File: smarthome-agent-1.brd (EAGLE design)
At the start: 100 x 80 mm, 7 parts, among them IC2 7808T, Q1 16Mhz, U1 ATMEGA328P_PDIP_EZ

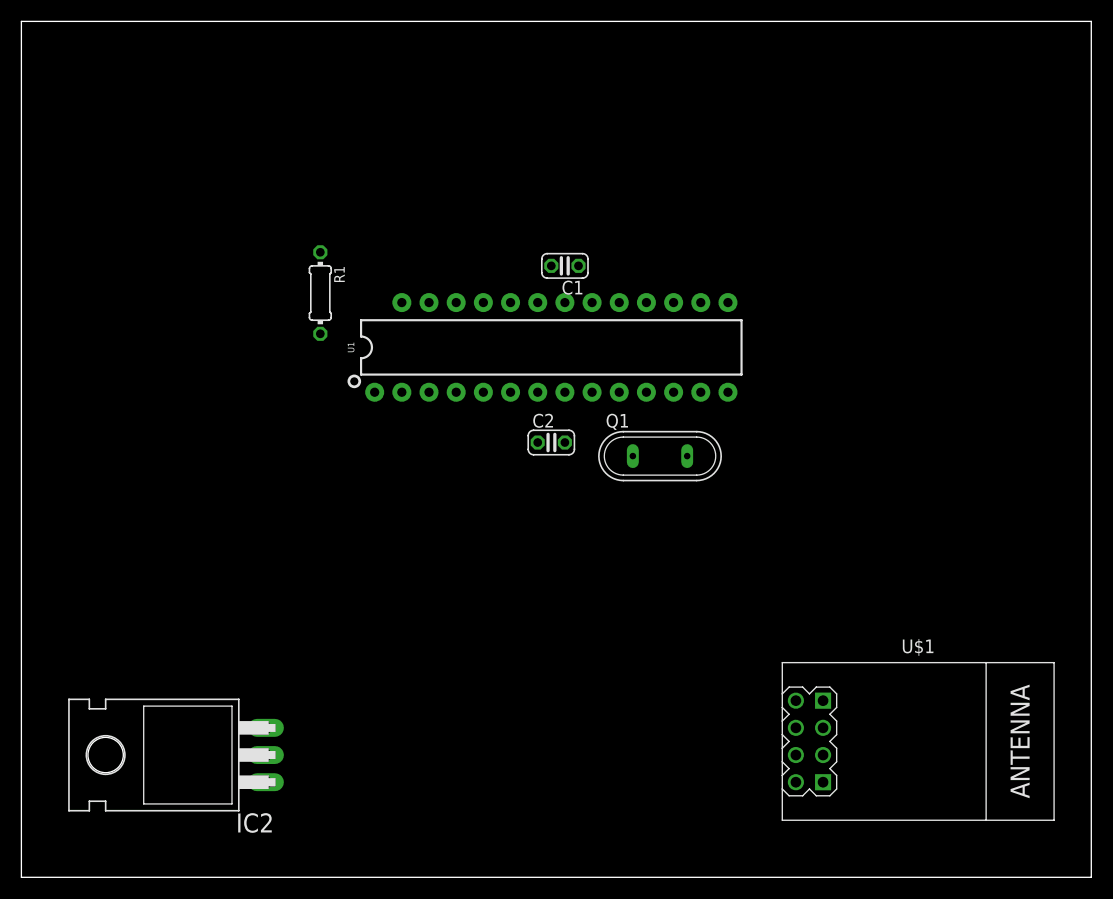
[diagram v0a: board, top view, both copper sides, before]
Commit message: Add board
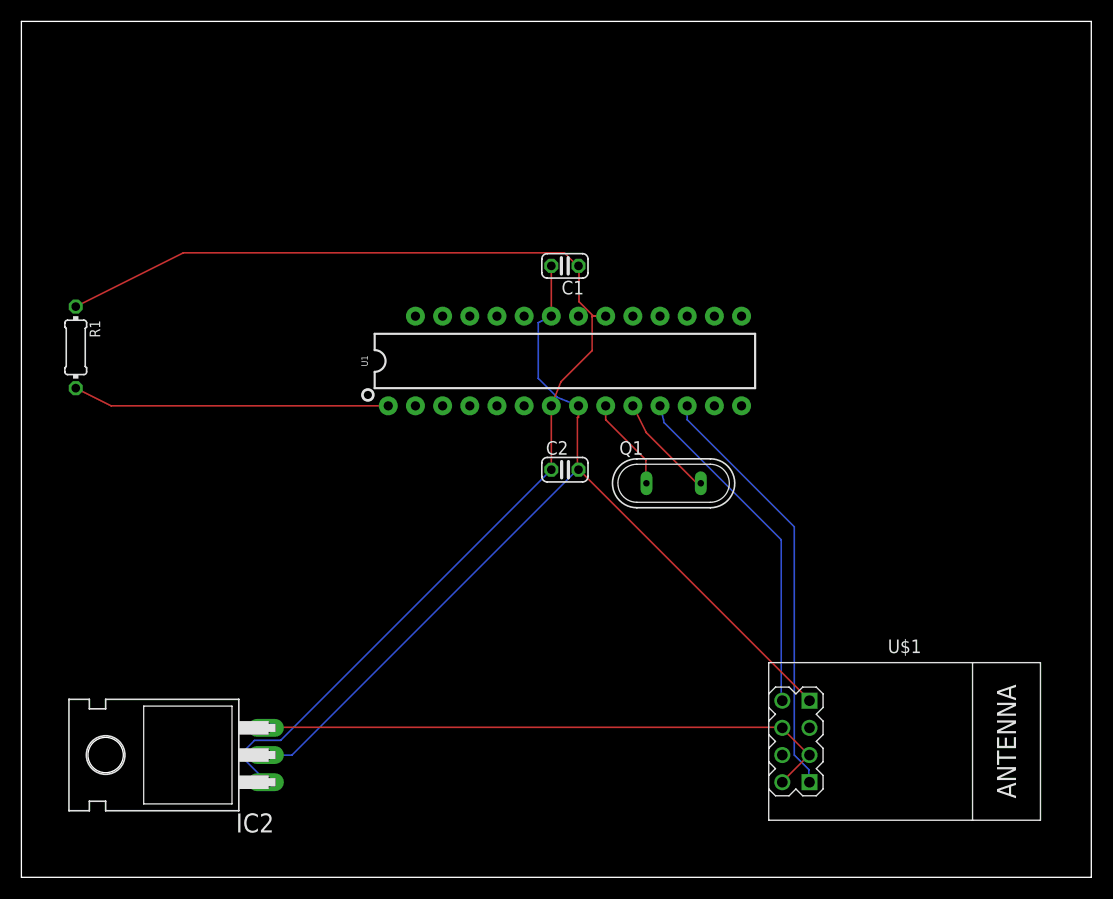
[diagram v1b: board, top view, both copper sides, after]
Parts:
- moved R1 23.4 mm to (5.08, 49.5)
- moved Q1 2.84 mm to (61.0, 36.8)
- moved C2 2.84 mm to (50.8, 38.1)
- moved U1 1.80 mm to (50.8, 48.3)
- moved U$1 1.27 mm to (82.5, 12.7)
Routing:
- net VCC: track 0.00 -> 115.4 mm
- net AGND: track 0.00 -> 92.9 mm
- net N$2: track 0.00 -> 55.5 mm
- net N$6: track 0.00 -> 39.9 mm
- net N$5: track 0.00 -> 32.2 mm
- net N$1: track 0.00 -> 29.6 mm
- net N$4: track 0.00 -> 9.85 mm
- net N$3: track 0.00 -> 8.82 mm

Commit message: Update board to use one layer
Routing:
- net AGND: track 92.9 -> 127.9 mm
- net VCC: track 115.4 -> 122.5 mm
- net N$6: track 39.9 -> 42.1 mm

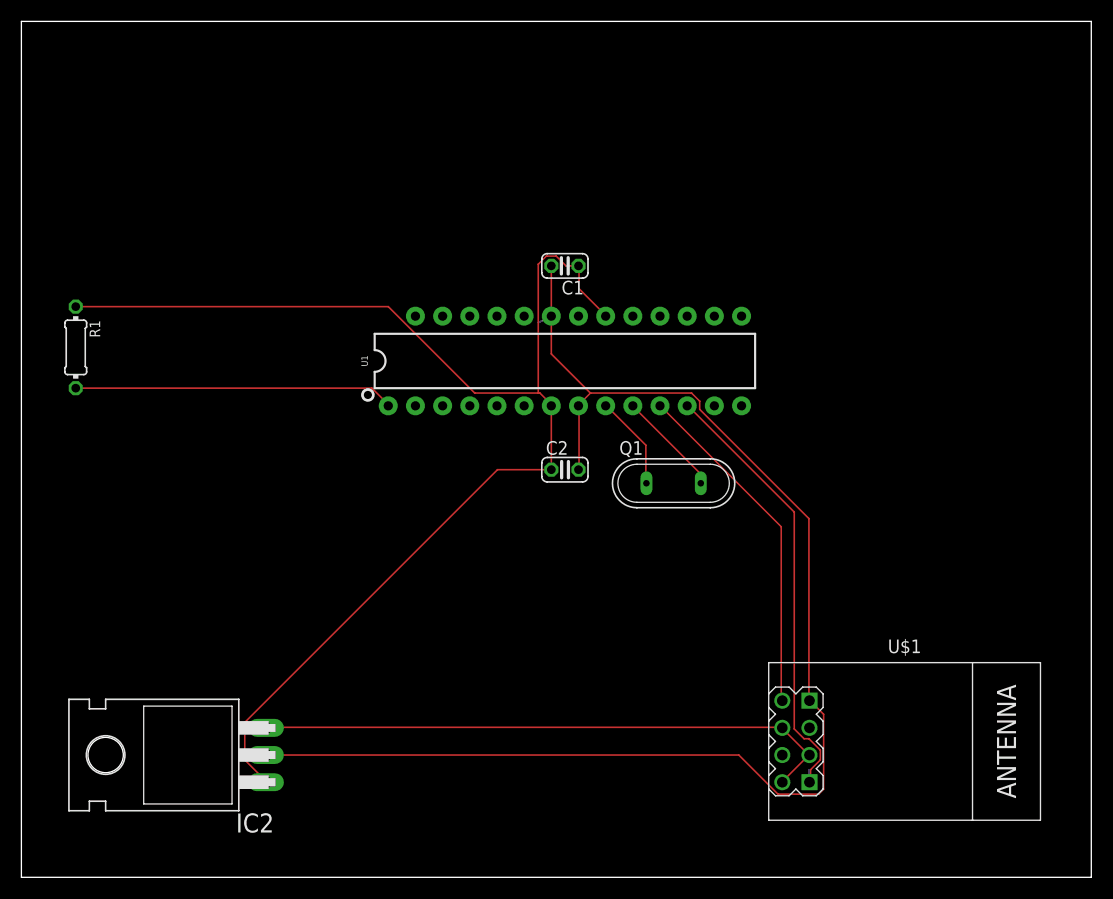
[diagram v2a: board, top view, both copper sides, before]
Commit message: Add IDC socket and USB
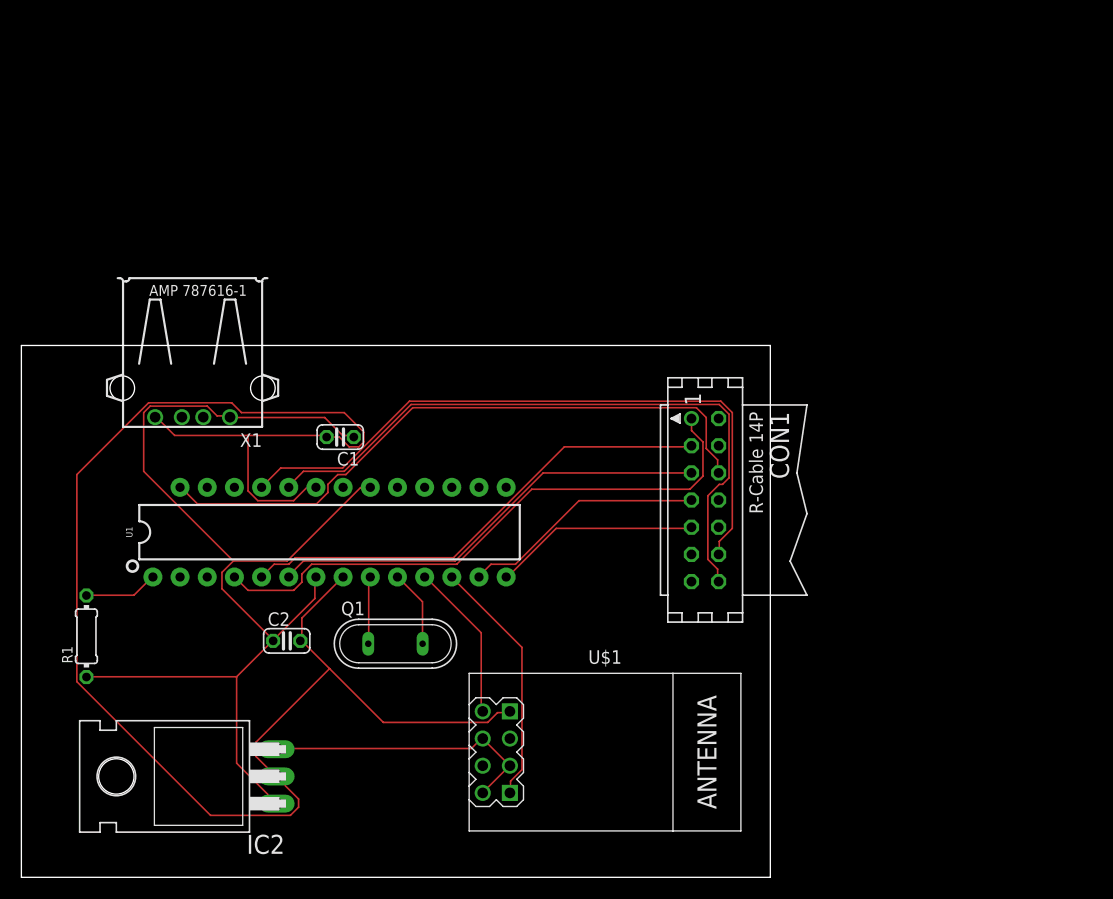
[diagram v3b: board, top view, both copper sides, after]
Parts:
- added CON1: (no value), con-harting:CON14
- added X1: (no value), con-amp:USB
- moved C2 30.5 mm to (24.8, 22.1)
- moved Q1 30.0 mm to (35.0, 21.8)
- moved U$1 28.0 mm to (54.5, 11.7)
- moved U1 27.2 mm to (28.8, 32.3)
- moved R1 27.0 mm to (6.08, 22.5), turned to 90 degrees
- moved C1 26.4 mm to (29.8, 41.1)
- moved IC2 2.24 mm to (13.7, 9.43)
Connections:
- removed net AGND: C1.2, C2.2, IC2.2, U$1.A1, U1.22, U1.8
- removed net VCC: C1.1, C2.1, IC2.1, R1.1, U1.20, U1.7
- new net N$10: CON1.7, U1.13
- new net N$11: CON1.14, U1.23
- new net N$12: CON1.12, U1.24
- new net N$13: CON1.10, U1.25
- new net N$14: CON1.8, U1.26
- new net N$15: CON1.6, U1.27
- new net N$16: CON1.9, U1.14
- new net N$17: C1.1, C2.1, IC2.1, R1.1, U1.20, U1.7, X1.1
- new net N$18: C1.2, C2.2, IC2.2, U$1.A1, U1.22, U1.8, X1.4
- new net N$7: CON1.1, U1.4
- new net N$8: CON1.3, U1.5
- new net N$9: CON1.5, U1.6
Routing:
- net N$18: track 0.00 -> 158.8 mm
- net AGND: track 127.9 -> 0.00 mm
- net VCC: track 122.5 -> 0.00 mm
- net N$17: track 0.00 -> 103.9 mm
- net N$11: track 0.00 -> 61.9 mm
- net N$12: track 0.00 -> 61.5 mm
- net N$15: track 0.00 -> 60.0 mm
- net N$7: track 0.00 -> 55.0 mm
- net N$8: track 0.00 -> 45.3 mm
- net N$9: track 0.00 -> 41.7 mm
- net N$2: track 55.5 -> 26.9 mm
- net N$1: track 30.0 -> 6.92 mm
- net N$10: track 0.00 -> 22.9 mm
- net N$16: track 0.00 -> 19.3 mm
- net N$6: track 42.1 -> 23.4 mm
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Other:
- board size 100 x 80 mm -> 70 x 49.7 mm

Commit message: Update board routing
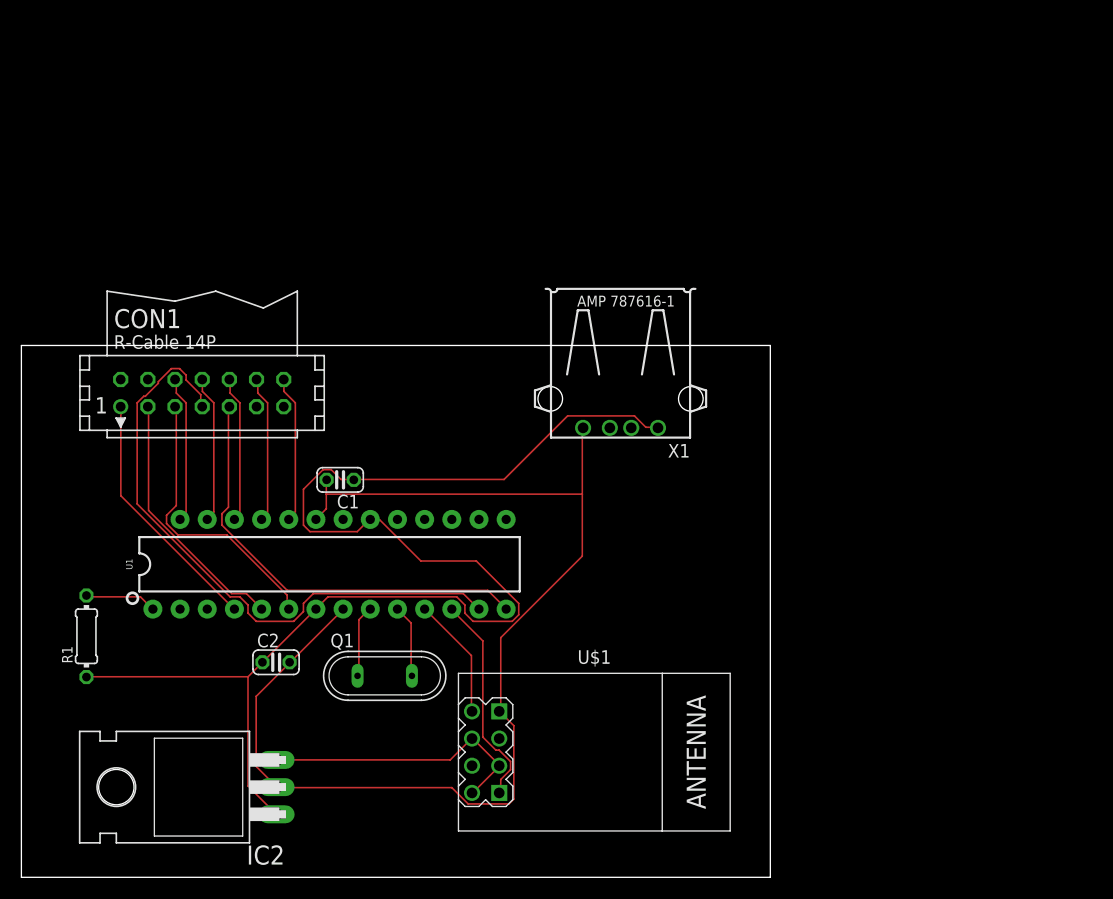
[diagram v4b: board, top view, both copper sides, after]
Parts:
- moved CON1 48.1 mm to (16.9, 45.3), turned to 0 degrees
- moved X1 40.0 mm to (56.0, 55.0)
- moved C1 4.00 mm to (29.8, 37.1)
- moved Q1 3.16 mm to (34.0, 18.8)
- moved U1 3.00 mm to (28.8, 29.3)
- moved C2 2.24 mm to (23.8, 20.1)
- moved IC2 1.00 mm to (13.7, 8.43)
- moved U$1 1.00 mm to (53.5, 11.7)
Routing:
- net N$18: track 158.8 -> 110.4 mm
- net N$11: track 61.9 -> 13.8 mm
- net N$12: track 61.5 -> 13.8 mm
- net N$15: track 60.0 -> 13.8 mm
- net N$10: track 22.9 -> 58.4 mm
- net N$7: track 55.0 -> 23.3 mm
- net N$16: track 19.3 -> 41.2 mm
- net N$8: track 45.3 -> 24.1 mm
- net N$17: track 103.9 -> 124.9 mm
- net N$9: track 41.7 -> 26.8 mm
- net N$14: track 0.00 -> 13.8 mm
- net N$13: track 0.00 -> 13.7 mm
- net N$5: track 14.9 -> 11.4 mm
- net N$6: track 23.4 -> 20.1 mm
- net N$2: track 26.9 -> 26.3 mm

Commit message: HOME-49 - Cleanup circuit and board design for production
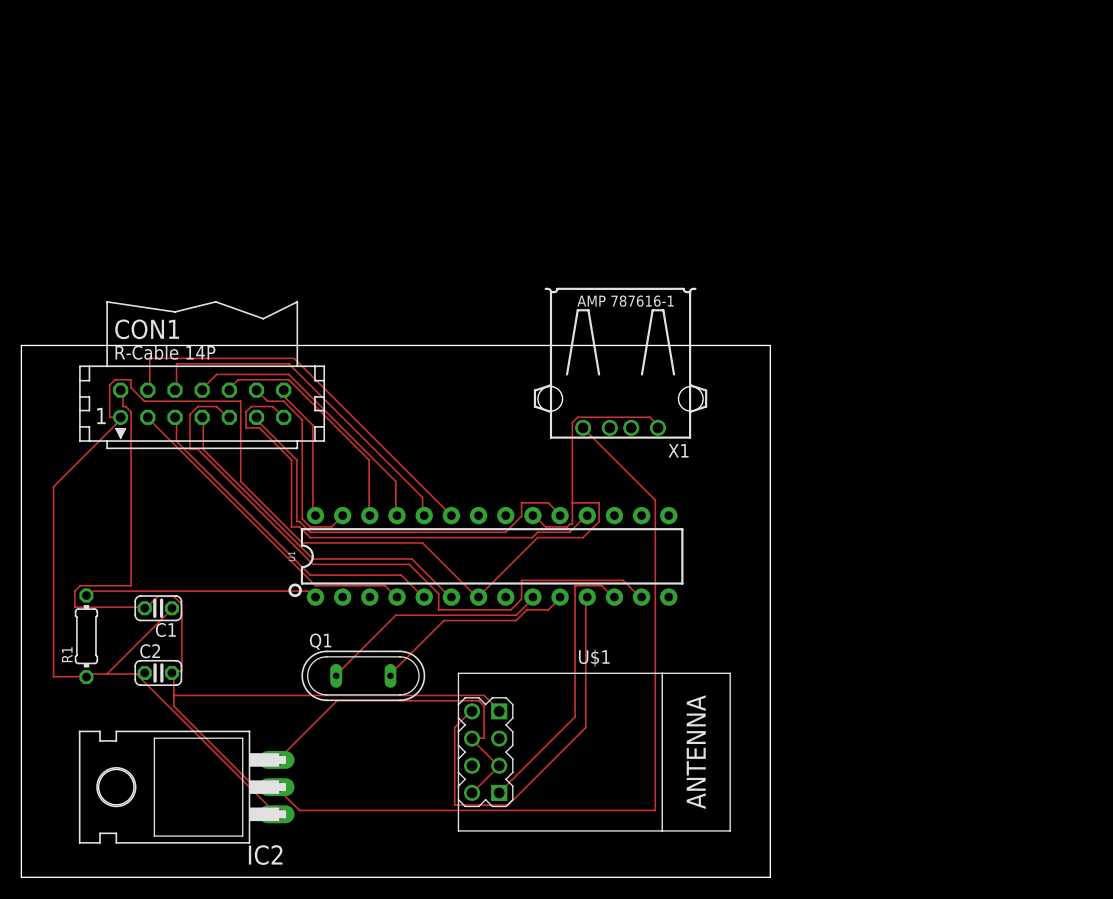
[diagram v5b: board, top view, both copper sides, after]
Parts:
- U1: value ATMEGA328P_PDIP_EZ -> 328P; device SparkFun-IC-Microcontroller:DIP28-SIMON-KIT -> SparkFun-IC-Microcontroller:DIP28
- moved C1 20.8 mm to (12.8, 25.1)
- moved U1 15.2 mm to (44.0, 30.0)
- moved C2 11.0 mm to (12.8, 19.1)
- moved Q1 2.00 mm to (32.0, 18.8)
- moved CON1 1.00 mm to (16.9, 44.3)
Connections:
- new net N$19: CON1.13, U1.18
- new net N$20: CON1.14, U1.28
- net N$10: now also CON1.8, U1.25; no longer CON1.7, U1.13
- net N$11: now also CON1.12, U1.27; no longer CON1.14, U1.23
- net N$12: now also CON1.3, U1.4; no longer CON1.12, U1.24
- net N$13: now also CON1.5, U1.5; no longer CON1.10, U1.25
- net N$14: now also CON1.7, U1.6; no longer CON1.8, U1.26
- net N$15: now also CON1.9, U1.13; no longer CON1.6, U1.27
- net N$16: now also CON1.11, U1.19; no longer CON1.9, U1.14
- net N$17: now also CON1.1
- net N$18: now also CON1.2; no longer U1.22, U1.8
- net N$7: now also CON1.10, U1.26; no longer CON1.1, U1.4
- net N$8: now also CON1.4, U1.23; no longer CON1.3, U1.5
- net N$9: now also CON1.6, U1.24; no longer CON1.5, U1.6
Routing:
- net N$18: track 110.4 -> 165.8 mm
- net N$19: track 0.00 -> 46.3 mm
- net N$15: track 13.8 -> 59.8 mm
- net N$10: track 58.4 -> 26.1 mm
- net N$17: track 124.9 -> 155.6 mm
- net N$5: track 11.4 -> 37.0 mm
- net N$14: track 13.8 -> 31.9 mm
- net N$13: track 13.7 -> 31.4 mm
- net N$12: track 13.8 -> 30.3 mm
- net N$1: track 6.79 -> 21.8 mm
- net N$4: track 6.79 -> 21.5 mm
- net N$8: track 24.1 -> 37.3 mm
- net N$20: track 0.00 -> 13.1 mm
- net N$3: track 6.80 -> 19.0 mm
- net N$2: track 26.3 -> 33.2 mm
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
